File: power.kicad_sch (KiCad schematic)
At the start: 29 parts, among them U33001 MC7805

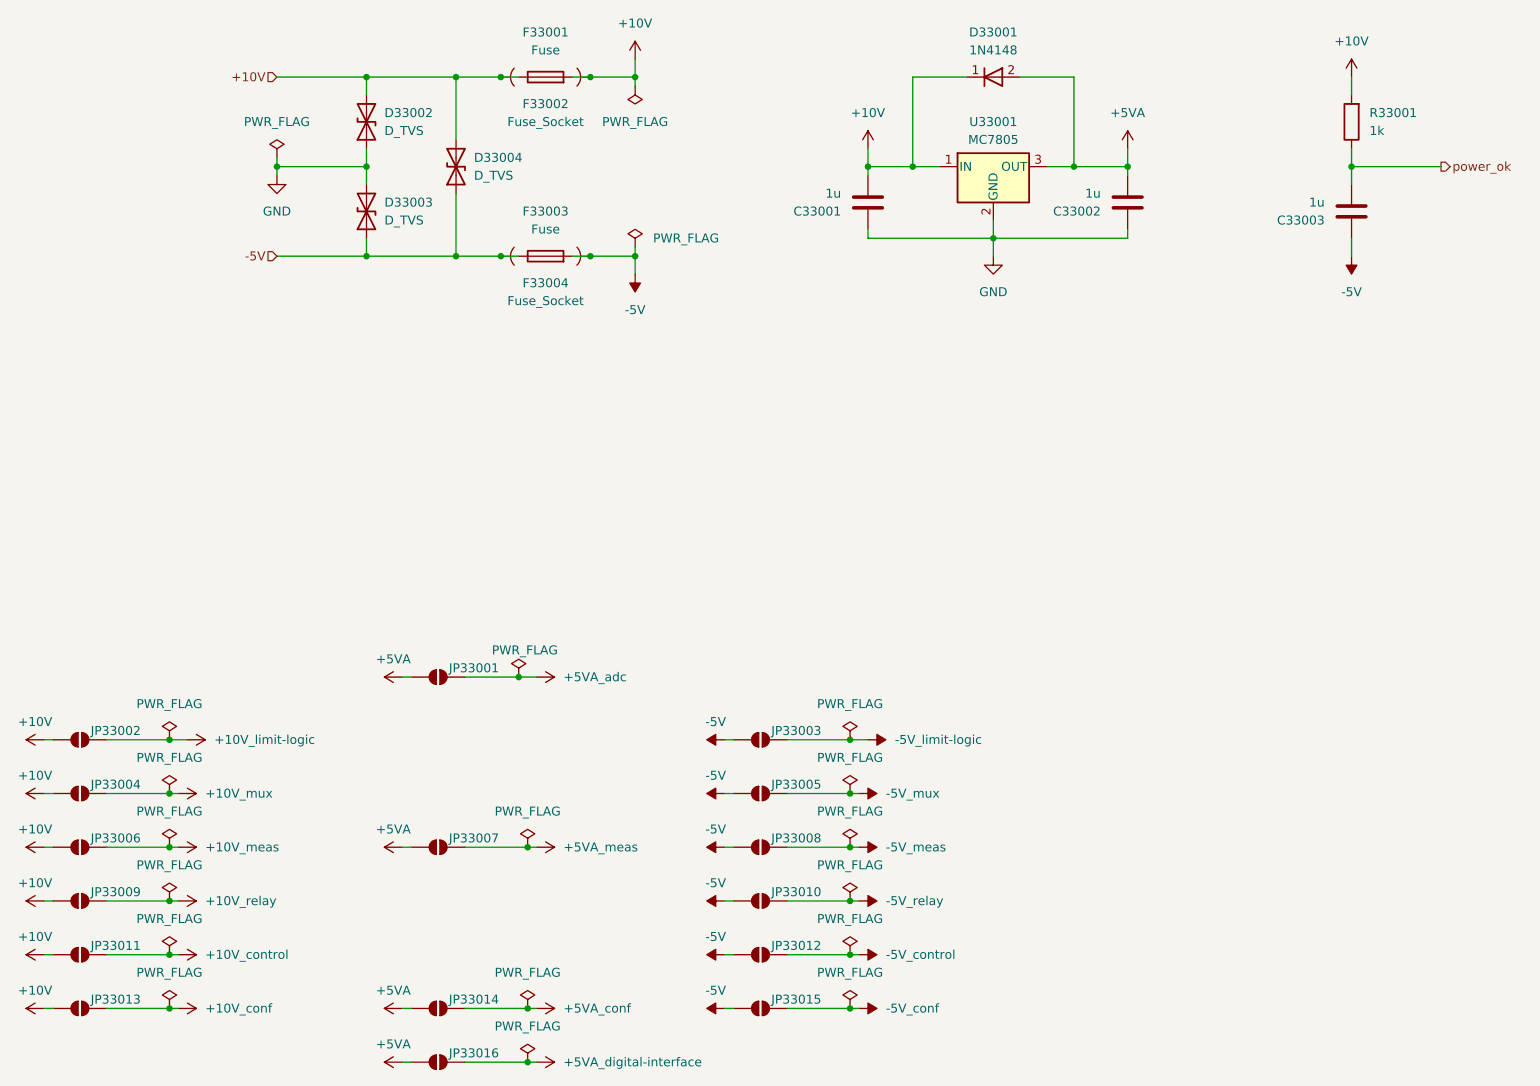
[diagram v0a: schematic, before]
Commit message: add pss 3dmodels and testpoints
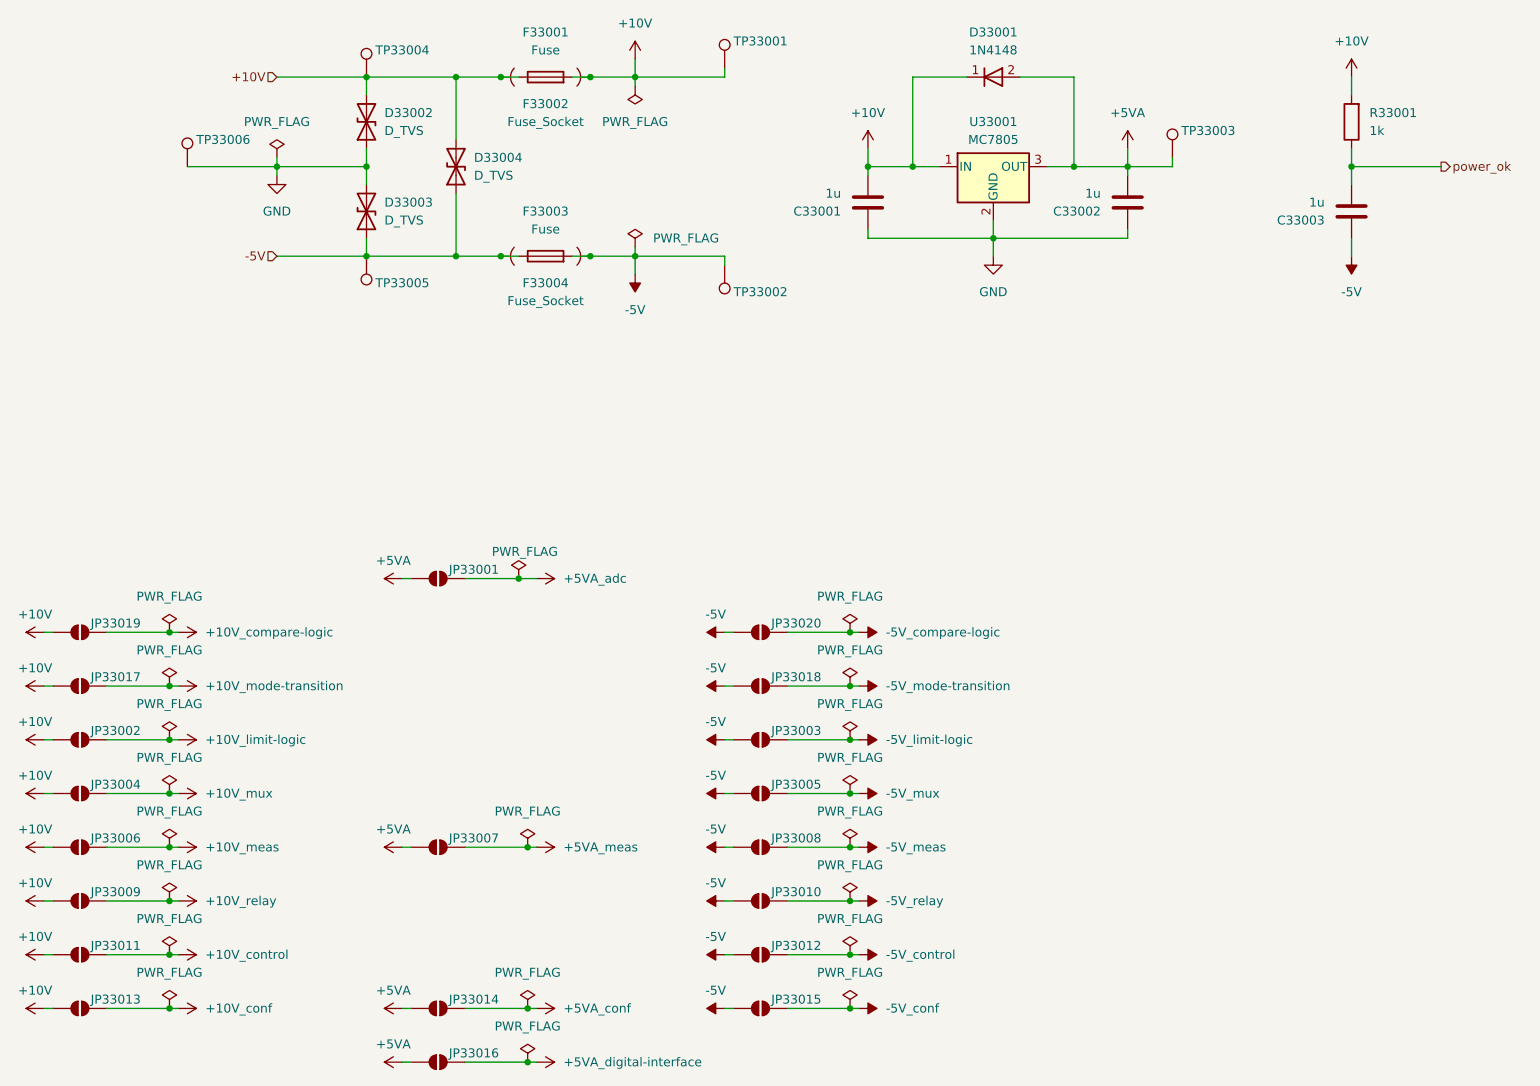
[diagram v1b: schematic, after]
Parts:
- added JP33017, JP33018, JP33019, JP33020: SolderJumper_2_Open, Jumper:SolderJumper-2_P1.3mm_Open_RoundedPad1.0x1.5mm, symbol Jumper:SolderJumper_2_Open
- added TP33001, TP33002, TP33003, TP33004, TP33005, TP33006: ~, pss:TP_0805_2012Metric, symbol Connector:TestPoint
- F33002, F33004: footprint Fuse:FuseHolder_Blade_ATO_Littelfuse_FLR_178.6165 -> pss:FuseHolder_Blade_ATO_Littelfuse_FLR_178.6165
- JP33001, JP33002, JP33003, JP33004, JP33005, JP33006, JP33007, JP33008, JP33009, JP33010, JP33011, JP33012, JP33013, JP33014, JP33015, JP33016: footprint (none) -> Jumper:SolderJumper-2_P1.3mm_Open_RoundedPad1.0x1.5mm
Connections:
- net +10V: now also JP33017.1 (A), JP33019.1 (A), TP33001.1, TP33004.1
- net +5VA: now also TP33003.1
- net -5V: now also JP33018.1 (A), JP33020.1 (A), TP33002.1, TP33005.1
- net GND: now also TP33006.1
- new net +10V_compare-logic: JP33019.2 (B)
- new net +10V_mode-transition: JP33017.2 (B)
- new net -5V_compare-logic: JP33020.2 (B)
- new net -5V_mode-transition: JP33018.2 (B)
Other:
- moved on the sheet: JP33001

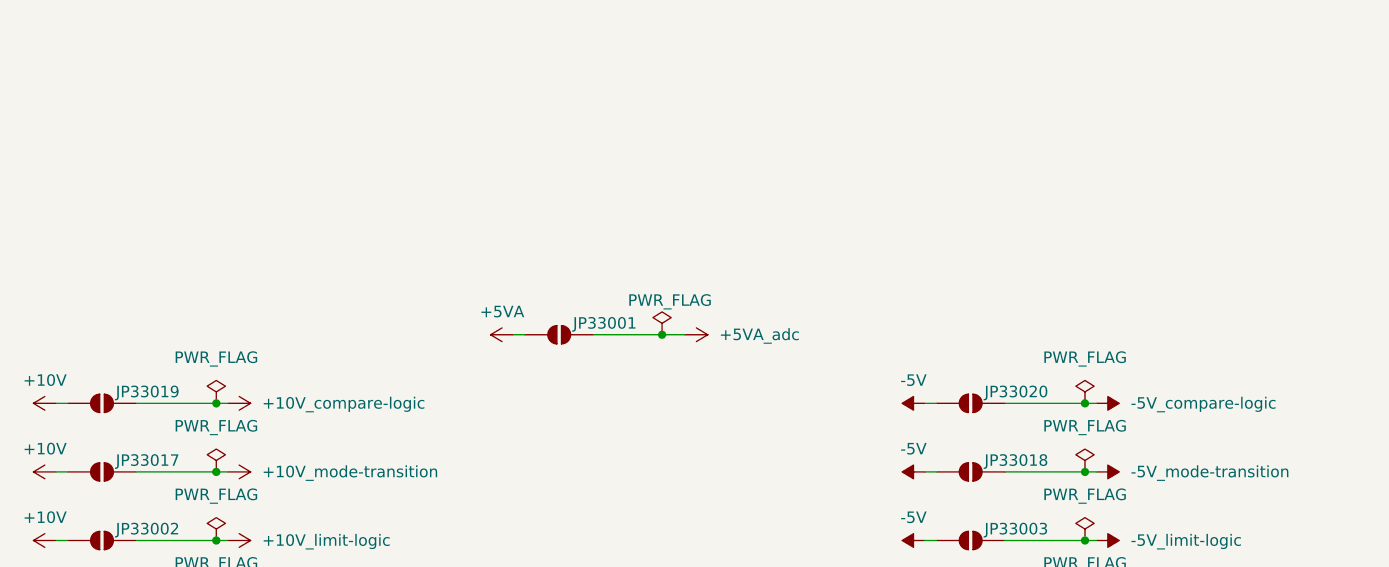
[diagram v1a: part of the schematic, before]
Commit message: add bias separate power supply net
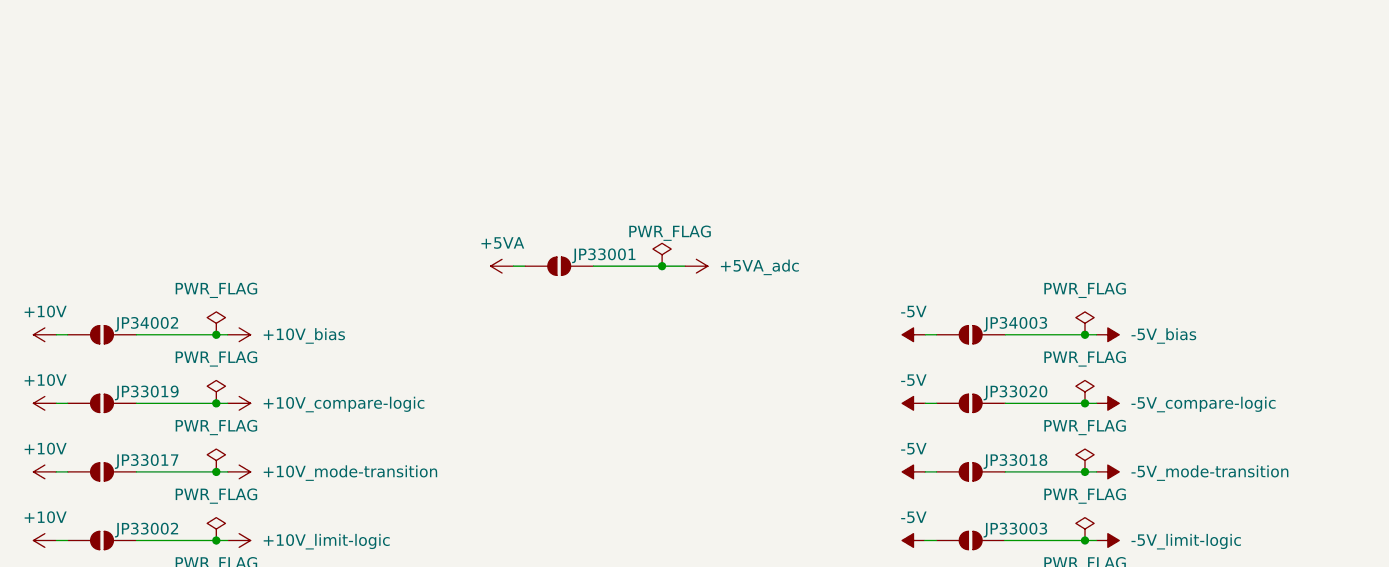
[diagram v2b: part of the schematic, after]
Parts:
- added JP34002, JP34003: SolderJumper_2_Open, Jumper:SolderJumper-2_P1.3mm_Open_RoundedPad1.0x1.5mm, symbol Jumper:SolderJumper_2_Open
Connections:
- net +10V: now also JP34002.1 (A)
- net -5V: now also JP34003.1 (A)
- new net +10V_bias: JP34002.2 (B)
- new net -5V_bias: JP34003.2 (B)
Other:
- moved on the sheet: JP33001

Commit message: edit pss reannotate entire schematic
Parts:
- U33001: MPN MC7805BDTG -> MC7805BDTG

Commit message: edit pss symbol library: export all schematic symbols to library 'pss' and update symbol link
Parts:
- D33001: symbol Device:D -> pss:D
- D33002, D33003, D33004: symbol Device:D_TVS -> pss:D_TVS
- F33001, F33003: symbol Device:Fuse -> pss:Fuse
- JP33001, JP33002, JP33003, JP33004, JP33005, JP33006, JP33007, JP33008, JP33009, JP33010, JP33011, JP33012, JP33013, JP33014, JP33015, JP33016, JP33017, JP33018, JP33019, JP33020, JP34002, JP34003: symbol Jumper:SolderJumper_2_Open -> pss:SolderJumper_2_Open
- TP33001, TP33002, TP33003, TP33004, TP33005, TP33006: symbol Connector:TestPoint -> pss:TestPoint
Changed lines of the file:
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@@
 	)
 	(symbol
-		(lib_id "Jumper:SolderJumper_2_Open")
+		(lib_id "pss:SolderJumper_2_Open")
 		(at 86.36 160.02 0)
 		(unit 1)
@@
 	)
 	(symbol
-		(lib_id "Connector:TestPoint")
+		(lib_id "pss:TestPoint")
 		(at 50.8 63.5 0)
 		(unit 1)
@@
 	)
 	(symbol
-		(lib_id "Jumper:SolderJumper_2_Open")
+		(lib_id "pss:SolderJumper_2_Open")
 		(at 132.08 137.16 0)
 		(unit 1)
@@
 	)
 	(symbol
-		(lib_id "Device:D_TVS")
+		(lib_id "pss:D_TVS")
 		(at 76.2 57.15 90)
 		(unit 1)
@@
 	)
 	(symbol
-		(lib_id "Jumper:SolderJumper_2_Open")
+		(lib_id "pss:SolderJumper_2_Open")
 		(at 132.08 144.78 0)
 		(unit 1)
@@
 	)
 	(symbol
-		(lib_id "Jumper:SolderJumper_2_Open")
+		(lib_id "pss:SolderJumper_2_Open")
 		(at 35.56 182.88 0)
 		(unit 1)
@@
 	)
 	(symbol
-		(lib_id "Connector:TestPoint")
+		(lib_id "pss:TestPoint")
 		(at 76.2 50.8 0)
 		(unit 1)
@@
 	)
 	(symbol
-		(lib_id "Device:D")
+		(lib_id "pss:D")
 		(at 165.1 50.8 0)
 		(unit 1)
@@
 	)
 	(symbol
-		(lib_id "Jumper:SolderJumper_2_Open")
+		(lib_id "pss:SolderJumper_2_Open")
 		(at 86.36 114.3 0)
 		(unit 1)
@@
 	)
 	(symbol
-		(lib_id "Connector:TestPoint")
+		(lib_id "pss:TestPoint")
 		(at 127 49.53 0)
 		(unit 1)
@@
 	)
 	(symbol
-		(lib_id "Jumper:SolderJumper_2_Open")
+		(lib_id "pss:SolderJumper_2_Open")
 		(at 35.56 121.92 0)
 		(unit 1)
@@
 	)
 	(symbol
-		(lib_id "power:+5VA")
+		(lib_id "pss:+5VA")
 		(at 81.28 160.02 90)
 		(unit 1)
@@
 	)
 	(symbol
-		(lib_id "power:+5VA")
+		(lib_id "pss:+5VA")
 		(at 81.28 182.88 90)
 		(unit 1)
@@
 	)
 	(symbol
-		(lib_id "Device:Fuse")
+		(lib_id "pss:Fuse")
 		(at 101.6 50.8 90)
 		(unit 1)
@@
 	)
 	(symbol
-		(lib_id "Jumper:SolderJumper_2_Open")
+		(lib_id "pss:SolderJumper_2_Open")
 		(at 132.08 152.4 0)
 		(unit 1)
@@
 	)
 	(symbol
-		(lib_id "Jumper:SolderJumper_2_Open")
+		(lib_id "pss:SolderJumper_2_Open")
 		(at 35.56 144.78 0)
 		(unit 1)
@@
 	)
 	(symbol
-		(lib_id "Jumper:SolderJumper_2_Open")
+		(lib_id "pss:SolderJumper_2_Open")
 		(at 86.36 190.5 0)
 		(unit 1)
@@
 	)
 	(symbol
-		(lib_id "Jumper:SolderJumper_2_Open")
+		(lib_id "pss:SolderJumper_2_Open")
 		(at 132.08 167.64 0)
 		(unit 1)
@@
 	)
 	(symbol
-		(lib_id "Connector:TestPoint")
+		(lib_id "pss:TestPoint")
 		(at 190.5 62.23 0)
 		(unit 1)
@@
 	)
 	(symbol
-		(lib_id "Device:Fuse")
+		(lib_id "pss:Fuse")
 		(at 101.6 76.2 90)
 		(unit 1)
@@
 	)
 	(symbol
-		(lib_id "Jumper:SolderJumper_2_Open")
+		(lib_id "pss:SolderJumper_2_Open")
 		(at 35.56 137.16 0)
 		(unit 1)
@@
 	)
 	(symbol
-		(lib_id "Jumper:SolderJumper_2_Open")
+		(lib_id "pss:SolderJumper_2_Open")
 		(at 35.56 175.26 0)
 		(unit 1)
@@
 	)
 	(symbol
-		(lib_id "Jumper:SolderJumper_2_Open")
+		(lib_id "pss:SolderJumper_2_Open")
 		(at 35.56 129.54 0)
 		(unit 1)
@@
 	)
 	(symbol
-		(lib_id "Jumper:SolderJumper_2_Open")
+		(lib_id "pss:SolderJumper_2_Open")
 		(at 35.56 152.4 0)
 		(unit 1)
@@
 	)
 	(symbol
-		(lib_id "Jumper:SolderJumper_2_Open")
+		(lib_id "pss:SolderJumper_2_Open")
 		(at 35.56 167.64 0)
 		(unit 1)
@@
 	)
 	(symbol
-		(lib_id "power:+5VA")
+		(lib_id "pss:+5VA")
 		(at 184.15 60.96 0)
 		(unit 1)
@@
 	)
 	(symbol
-		(lib_id "power:+5VA")
+		(lib_id "pss:+5VA")
 		(at 81.28 190.5 90)
 		(unit 1)
@@
 	)
 	(symbol
-		(lib_id "Jumper:SolderJumper_2_Open")
+		(lib_id "pss:SolderJumper_2_Open")
 		(at 86.36 182.88 0)
 		(unit 1)
@@
 	)
 	(symbol
-		(lib_id "Connector:TestPoint")
+		(lib_id "pss:TestPoint")
 		(at 76.2 76.2 0)
 		(mirror x)
@@
 	)
 	(symbol
-		(lib_id "power:+5VA")
+		(lib_id "pss:+5VA")
 		(at 81.28 114.3 90)
 		(unit 1)
@@
 	)
 	(symbol
-		(lib_id "Device:D_TVS")
+		(lib_id "pss:D_TVS")
 		(at 76.2 69.85 90)
 		(unit 1)
@@
 	)
 	(symbol
-		(lib_id "Jumper:SolderJumper_2_Open")
+		(lib_id "pss:SolderJumper_2_Open")
 		(at 35.56 160.02 0)
 		(unit 1)
@@
 	)
 	(symbol
-		(lib_id "Jumper:SolderJumper_2_Open")
+		(lib_id "pss:SolderJumper_2_Open")
 		(at 132.08 129.54 0)
 		(unit 1)
@@
 	)
 	(symbol
-		(lib_id "Jumper:SolderJumper_2_Open")
+		(lib_id "pss:SolderJumper_2_Open")
 		(at 132.08 160.02 0)
 		(unit 1)
@@
 	)
 	(symbol
-		(lib_id "Jumper:SolderJumper_2_Open")
+		(lib_id "pss:SolderJumper_2_Open")
 		(at 132.08 121.92 0)
 		(unit 1)
@@
 	)
 	(symbol
-		(lib_id "Jumper:SolderJumper_2_Open")
+		(lib_id "pss:SolderJumper_2_Open")
 		(at 132.08 182.88 0)
 		(unit 1)
@@
 	)
 	(symbol
-		(lib_id "Device:D_TVS")
+		(lib_id "pss:D_TVS")
 		(at 88.9 63.5 90)
 		(unit 1)
@@
 	)
 	(symbol
-		(lib_id "Jumper:SolderJumper_2_Open")
+		(lib_id "pss:SolderJumper_2_Open")
 		(at 132.08 175.26 0)
 		(unit 1)
@@
 	)
 	(symbol
-		(lib_id "Connector:TestPoint")
+		(lib_id "pss:TestPoint")
 		(at 127 77.47 0)
 		(mirror x)
